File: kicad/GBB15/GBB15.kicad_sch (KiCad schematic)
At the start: 70 parts, among them J1 CAN_IN, J10 USB_C_Receptacle_USB2.0, J2 CAN_OUT, J3 M0_THERM, J4 M1_THERM, J5 Conn_01x04_Male, J6 Conn_01x04_Male, J7 ENDSTOP1, J8 ENDSTOP2, SW1 SW_Push, SW2 SW_Push, U1 TMC2209-LA-T, U2 STM32G0B1CEU6, U3 TMC2209-LA-T, U4 TCAN334, U5 NCP730BMT330TBG, Y1 Crystal_GND24

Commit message: PCB cleanup
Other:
- note added: "USB Type-C upright LCSC part#: C2763103 (1mm PCB) C3039300 C3039301 (1mm PCB) C3151747 C3151746"
- note removed: "Achtung mit UARTS im Bootloader Modus"
- note removed: "Motor A/B statt 0/1"
- note removed: "USB Type-C upright C2763103 (1mm PCB) C3039300 C3039301 (1mm PCB) C3151747 C3151746"
- note removed: "Umbennnen"
- note removed: "serial port"
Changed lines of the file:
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@@
-    (effects (font (size 1.27 1.27)) (justify left bottom))
-  )
-  (text "Motor A/B statt 0/1" (at 275.59 -13.97 0)
     (effects (font (size 1.27 1.27)) (justify left bottom))
   )
@@
   )
   (text "ADC" (at 246.38 146.05 0)
-    (effects (font (size 1.27 1.27)) (justify left bottom))
-  )
-  (text "serial port" (at 203.2 -26.67 0)
     (effects (font (size 1.27 1.27)) (justify left bottom))
   )
@@
   )
   (text "USART5_TX" (at 135.89 153.67 0)
-    (effects (font (size 1.27 1.27)) (justify left bottom))
-  )
-  (text "Umbennnen" (at 168.9067 -20.4934 0)
     (effects (font (size 1.27 1.27)) (justify left bottom))
   )
@@
     (effects (font (size 1.27 1.27)) (justify left bottom))
   )
-  (text "USB Type-C upright\nC2763103 (1mm PCB)\nC3039300\nC3039301 (1mm PCB)\nC3151747\nC3151746"
-    (at 214.63 -13.97 0)
+  (text "USB Type-C upright LCSC part#:\nC2763103 (1mm PCB)\nC3039300\nC3039301 (1mm PCB)\nC3151747\nC3151746"
+    (at 31.75 111.76 0)
     (effects (font (size 1.27 1.27)) (justify left bottom))
   )
@@
     (effects (font (size 1.27 1.27)) (justify left bottom))
   )
-  (text "Achtung mit UARTS im Bootloader Modus\n" (at 156.21 -2.54 0)
-    (effects (font (size 1.27 1.27)) (justify left bottom))
-  )

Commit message: Small changes in JST connector type
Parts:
- J5, J6: footprint Connector_JST:JST_XA_B04B-XASK-1_1x04_P2.50mm_Vertical -> Connector_JST:JST_XH_B4B-XH-A_1x04_P2.50mm_Vertical
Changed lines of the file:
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@@
       (effects (font (size 1.27 1.27)) (justify right))
     )
-    (property "Footprint" "Connector_JST:JST_XA_B04B-XASK-1_1x04_P2.50mm_Vertical" (id 2) (at 372.11 193.04 0)
+    (property "Footprint" "Connector_JST:JST_XH_B4B-XH-A_1x04_P2.50mm_Vertical" (id 2) (at 372.11 193.04 0)
       (effects (font (size 1.27 1.27)) hide)
     )
@@
       (effects (font (size 1.27 1.27)) (justify right))
     )
-    (property "Footprint" "Connector_JST:JST_XA_B04B-XASK-1_1x04_P2.50mm_Vertical" (id 2) (at 372.11 62.23 0)
+    (property "Footprint" "Connector_JST:JST_XH_B4B-XH-A_1x04_P2.50mm_Vertical" (id 2) (at 372.11 62.23 0)
       (effects (font (size 1.27 1.27)) hide)
     )
@@
     )
     (path "/9d8076e4-90bf-434d-b742-fd981c971465"
-      (reference "J5") (unit 1) (value "Conn_01x04_Male") (footprint "Connector_JST:JST_XA_B04B-XASK-1_1x04_P2.50mm_Vertical")
+      (reference "J5") (unit 1) (value "Conn_01x04_Male") (footprint "Connector_JST:JST_XH_B4B-XH-A_1x04_P2.50mm_Vertical")
     )
     (path "/3b24db73-62b8-474f-9981-d07b21e4d1b2"
-      (reference "J6") (unit 1) (value "Conn_01x04_Male") (footprint "Connector_JST:JST_XA_B04B-XASK-1_1x04_P2.50mm_Vertical")
+      (reference "J6") (unit 1) (value "Conn_01x04_Male") (footprint "Connector_JST:JST_XH_B4B-XH-A_1x04_P2.50mm_Vertical")
     )
     (path "/d1dfdd89-38c1-4297-bb44-8a8a1f194428"

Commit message: Added LCSC properties in schematic
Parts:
- C1, C17: LCSC (none) -> C3035369
- C10, C14, C22, C30: LCSC (none) -> C19666
- C11, C16, C18, C2, C21, C24, C26, C27, C28, C6, C7: LCSC (none) -> C57112
- C12, C15, C29, C8, C9: LCSC (none) -> C28323
- C13, C5: LCSC (none) -> C21122
- C3, C4: LCSC (none) -> C1653
- J1, J2: LCSC (none) -> C563821
- J10: LCSC (none) -> C3151747
- J3, J4, J7, J8: LCSC (none) -> C131337
- J5, J6: LCSC (none) -> C144395
- R1, R10, R2, R9: LCSC (none) -> C2934288
- R11, R12, R14, R20, R21, R22, R23, R5, R6: LCSC (none) -> C23162
- R13, R15: LCSC (none) -> C23186
- R16, R3, R4, R7, R8: LCSC (none) -> C25804
- R19: LCSC (none) -> C17909
- SW1, SW2: LCSC (none) -> C255802
- TH1: LCSC (none) -> C919169
- U1, U3: LCSC (none) -> C465949
- U2: LCSC (none) -> C2829190
- U4: LCSC (none) -> C165159
- U5: LCSC (none) -> C892821
- Y1: LCSC (none) -> C2682774

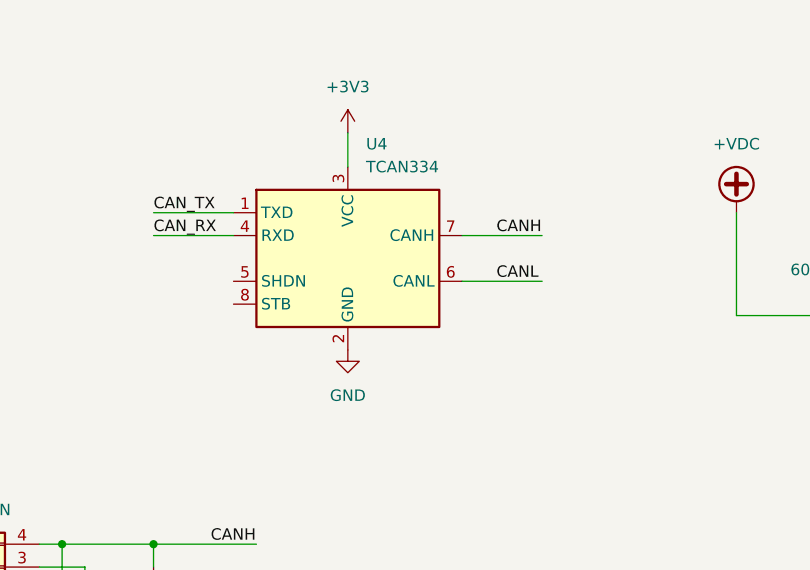
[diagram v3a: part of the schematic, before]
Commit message: Connected unconnected pads on TCAN334 to ground
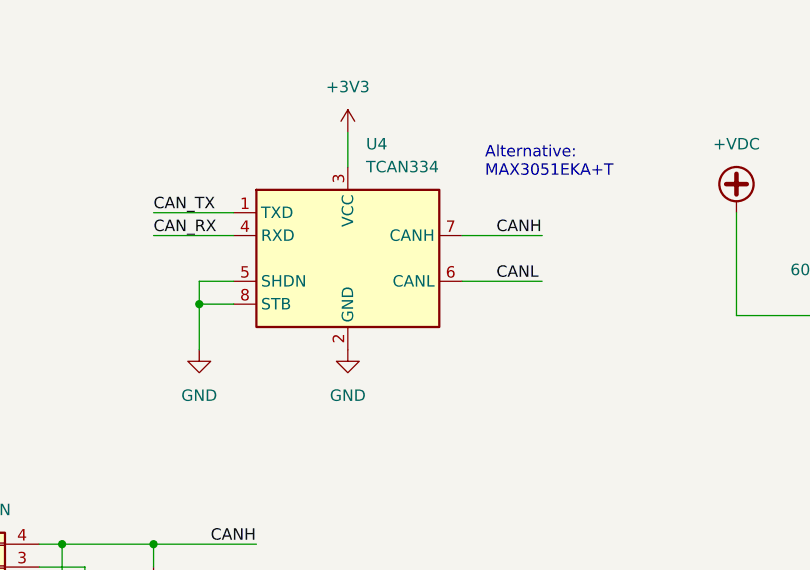
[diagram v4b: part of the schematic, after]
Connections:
- net GND: now also U4.5 (SHDN), U4.8 (STB)
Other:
- note added: "Alternative: MAX3051EKA+T"
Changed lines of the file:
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@@
   (junction (at 194.31 191.77) (diameter 0) (color 0 0 0 0)
   )
+  (junction (at 63.5 44.45) (diameter 0) (color 0 0 0 0)
+  )
   (junction (at 328.93 219.71) (diameter 0) (color 0 0 0 0)
   )
@@
     (stroke (width 0) (type default) (color 0 0 0 0))
   )
+  (wire (pts (xy 63.5 44.45) (xy 63.5 49.53))
+    (stroke (width 0) (type default) (color 0 0 0 0))
+  )
   (wire (pts (xy 48.26 71.12) (xy 58.42 71.12))
     (stroke (width 0) (type default) (color 0 0 0 0))
@@
     (stroke (width 0) (type default) (color 0 0 0 0))
   )
+  (wire (pts (xy 67.31 41.91) (xy 63.5 41.91))
+    (stroke (width 0) (type default) (color 0 0 0 0))
+  )
   (wire (pts (xy 344.17 154.94) (xy 344.17 156.21))
     (stroke (width 0) (type default) (color 0 0 0 0))
@@
     (stroke (width 0) (type default) (color 0 0 0 0))
   )
+  (wire (pts (xy 63.5 41.91) (xy 63.5 44.45))
+    (stroke (width 0) (type default) (color 0 0 0 0))
+  )
   (wire (pts (xy 292.1 72.39) (xy 295.91 72.39))
     (stroke (width 0) (type default) (color 0 0 0 0))
@@
     (stroke (width 0) (type default) (color 0 0 0 0))
   )
+  (wire (pts (xy 67.31 44.45) (xy 63.5 44.45))
+    (stroke (width 0) (type default) (color 0 0 0 0))
+  )
   (wire (pts (xy 303.53 64.77) (xy 311.15 64.77))
     (stroke (width 0) (type default) (color 0 0 0 0))
@@
     (effects (font (size 1.27 1.27)) (justify left bottom))
   )
+  (text "Alternative:\nMAX3051EKA+T" (at 95.25 30.48 0)
+    (effects (font (size 1.27 1.27)) (justify left bottom))
+  )
   (text "FDCAN2_RX" (at 152.4 146.05 0)
     (effects (font (size 1.27 1.27)) (justify left bottom))
@@
     (pin "1")
   )
+  (symbol (lib_id "power:GND") (at 63.5 49.53 0) (unit 1)
+    (in_bom yes) (on_board yes) (fields_autoplaced)
+    (property "Reference" "#PWR0164" (id 0) (at 63.5 55.88 0)
+      (effects (font (size 1.27 1.27)) hide)
+    )
+    (property "Value" "GND" (id 1) (at 63.5 54.61 0))
+    (property "Footprint" "" (id 2) (at 63.5 49.53 0)
+      (effects (font (size 1.27 1.27)) hide)
+    )
+    (property "Datasheet" "" (id 3) (at 63.5 49.53 0)
+      (effects (font (size 1.27 1.27)) hide)
+    )
+    (pin "1")
+  )
   (symbol (lib_id "Device:C") (at 354.33 160.02 180) (unit 1)
     (in_bom yes) (on_board yes)
@@
       (reference "#PWR0163") (unit 1) (value "+3V3") (footprint "")
     )
+    (path "/7c0fd88a-fa32-46d6-8af5-3806631ccf87"
+      (reference "#PWR0164") (unit 1) (value "GND") (footprint "")
+    )
     (path "/2357a709-2903-4077-9523-97359b4f842d"

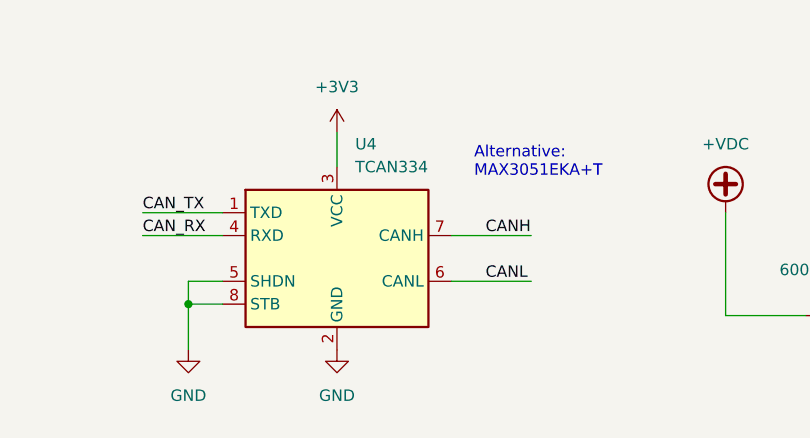
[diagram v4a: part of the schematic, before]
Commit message: Correct 100nF capacitor part number and changed to MAX3051 instead of TCAN334
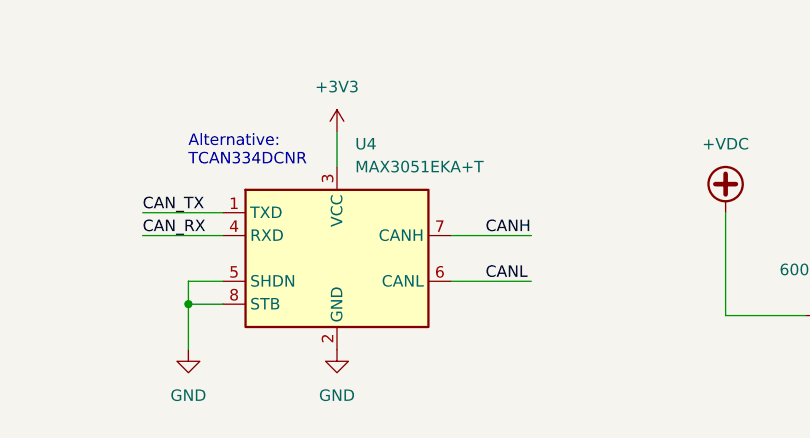
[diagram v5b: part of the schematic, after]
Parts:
- C11, C16, C18, C2, C21, C24, C26, C27, C28, C6, C7: LCSC C57112 -> C14663
- U4: value TCAN334 -> MAX3051EKA+T; LCSC C165159 -> C112005
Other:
- note added: "Alternative: TCAN334DCNR"
- note removed: "Alternative: MAX3051EKA+T"
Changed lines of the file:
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@@
     (effects (font (size 1.27 1.27)) (justify left bottom))
   )
-  (text "Alternative:\nMAX3051EKA+T" (at 95.25 30.48 0)
+  (text "Alternative:\nTCAN334DCNR\n" (at 63.5 29.21 0)
     (effects (font (size 1.27 1.27)) (justify left bottom))
   )
@@
       (effects (font (size 1.27 1.27)) hide)
     )
-    (property "LCSC" "C57112" (id 4) (at 118.11 123.19 0)
+    (property "LCSC" "C14663" (id 4) (at 118.11 123.19 0)
       (effects (font (size 1.27 1.27)) hide)
     )
@@
       (effects (font (size 1.27 1.27)) hide)
     )
-    (property "LCSC" "C57112" (id 4) (at 307.34 35.56 0)
+    (property "LCSC" "C14663" (id 4) (at 307.34 35.56 0)
       (effects (font (size 1.27 1.27)) hide)
     )
@@
       (effects (font (size 1.27 1.27)) (justify left))
     )
-    (property "Value" "TCAN334" (id 1) (at 82.0294 29.21 0)
+    (property "Value" "MAX3051EKA+T" (id 1) (at 82.0294 29.21 0)
       (effects (font (size 1.27 1.27)) (justify left))
     )
@@
       (effects (font (size 1.27 1.27)) hide)
     )
-    (property "LCSC" "C165159" (id 4) (at 82.0294 26.67 0)
+    (property "LCSC" "C112005" (id 4) (at 82.0294 26.67 0)
       (effects (font (size 1.27 1.27)) hide)
     )
@@
       (effects (font (size 1.27 1.27)) hide)
     )
-    (property "LCSC" "C57112" (id 4) (at 347.98 132.08 0)
+    (property "LCSC" "C14663" (id 4) (at 347.98 132.08 0)
       (effects (font (size 1.27 1.27)) hide)
     )
@@
       (effects (font (size 1.27 1.27)) hide)
     )
-    (property "LCSC" "C57112" (id 4) (at 128.27 123.19 0)
+    (property "LCSC" "C14663" (id 4) (at 128.27 123.19 0)
       (effects (font (size 1.27 1.27)) hide)
     )
@@
       (effects (font (size 1.27 1.27)) hide)
     )
-    (property "LCSC" "C57112" (id 4) (at 293.37 132.08 0)
+    (property "LCSC" "C14663" (id 4) (at 293.37 132.08 0)
       (effects (font (size 1.27 1.27)) hide)
     )
@@
       (effects (font (size 1.27 1.27)) hide)
     )
-    (property "LCSC" "C57112" (id 4) (at 72.39 242.57 0)
+    (property "LCSC" "C14663" (id 4) (at 72.39 242.57 0)
       (effects (font (size 1.27 1.27)) hide)
     )
@@
       (effects (font (size 1.27 1.27)) hide)
     )
-    (property "LCSC" "C57112" (id 4) (at 365.76 45.72 0)
+    (property "LCSC" "C14663" (id 4) (at 365.76 45.72 0)
       (effects (font (size 1.27 1.27)) hide)
     )
@@
       (effects (font (size 1.27 1.27)) hide)
     )
-    (property "LCSC" "C57112" (id 4) (at 72.39 201.93 0)
+    (property "LCSC" "C14663" (id 4) (at 72.39 201.93 0)
       (effects (font (size 1.27 1.27)) hide)
     )
@@
       (effects (font (size 1.27 1.27)) hide)
     )
-    (property "LCSC" "C57112" (id 4) (at 365.76 176.53 0)
+    (property "LCSC" "C14663" (id 4) (at 365.76 176.53 0)
       (effects (font (size 1.27 1.27)) hide)
     )
@@
       (effects (font (size 1.27 1.27)) hide)
     )
-    (property "LCSC" "C57112" (id 4) (at 307.34 166.37 0)
+    (property "LCSC" "C14663" (id 4) (at 307.34 166.37 0)
       (effects (font (size 1.27 1.27)) hide)
     )
@@
       (effects (font (size 1.27 1.27)) hide)
     )
-    (property "LCSC" "C57112" (id 4) (at 125.73 158.75 0)
+    (property "LCSC" "C14663" (id 4) (at 125.73 158.75 0)
       (effects (font (size 1.27 1.27)) hide)
     )
@@
     )
     (path "/1bcdfb0e-7d1c-413c-9751-c956c1d9a4e0"
-      (reference "U4") (unit 1) (value "TCAN334") (footprint "Package_TO_SOT_SMD:SOT-23-8")
+      (reference "U4") (unit 1) (value "MAX3051EKA+T") (footprint "Package_TO_SOT_SMD:SOT-23-8")
     )
     (path "/bab8dc9b-0be7-4bfb-810b-951e3d411197"

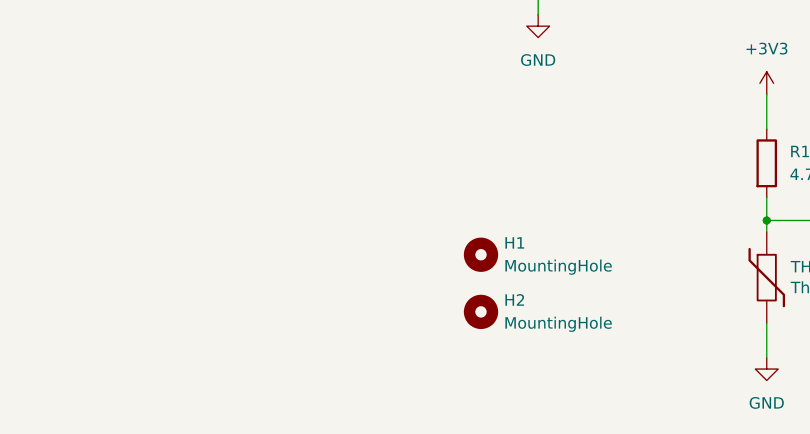
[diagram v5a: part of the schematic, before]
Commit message: Added tooling holes
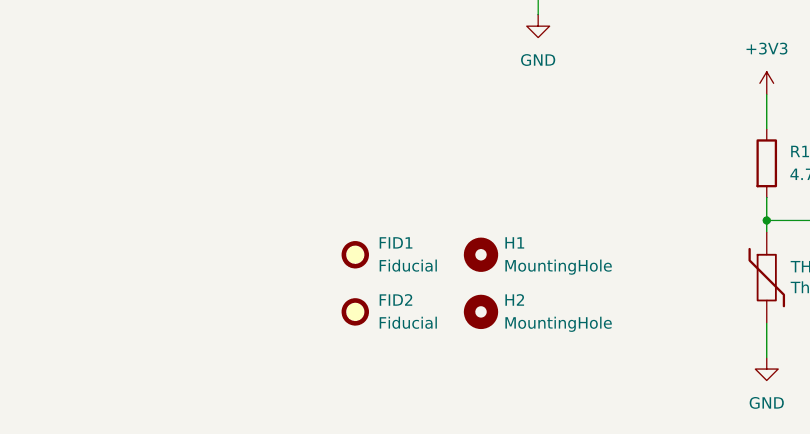
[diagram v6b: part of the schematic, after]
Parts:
- added FID1, FID2: Fiducial, Project:TOOLING-HOLE, symbol Mechanical:Fiducial
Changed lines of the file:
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@@
     (pin "2")
+  )
+  (symbol (lib_id "Mechanical:Fiducial") (at 157.48 256.54 0) (unit 1)
+    (in_bom yes) (on_board yes) (fields_autoplaced)
+    (property "Reference" "FID2" (id 0) (at 160.02 255.2699 0)
+      (effects (font (size 1.27 1.27)) (justify left))
+    )
+    (property "Value" "Fiducial" (id 1) (at 160.02 257.8099 0)
+      (effects (font (size 1.27 1.27)) (justify left))
+    )
+    (property "Footprint" "Project:TOOLING-HOLE" (id 2) (at 157.48 256.54 0)
+      (effects (font (size 1.27 1.27)) hide)
+    )
+    (property "Datasheet" "~" (id 3) (at 157.48 256.54 0)
+      (effects (font (size 1.27 1.27)) hide)
+    )
   )
   (symbol (lib_id "Device:C") (at 124.46 116.84 180) (unit 1)
@@
     (pin "2")
   )
+  (symbol (lib_id "Mechanical:Fiducial") (at 157.48 250.19 0) (unit 1)
+    (in_bom yes) (on_board yes) (fields_autoplaced)
+    (property "Reference" "FID1" (id 0) (at 160.02 248.9199 0)
+      (effects (font (size 1.27 1.27)) (justify left))
+    )
+    (property "Value" "Fiducial" (id 1) (at 160.02 251.4599 0)
+      (effects (font (size 1.27 1.27)) (justify left))
+    )
+    (property "Footprint" "Project:TOOLING-HOLE" (id 2) (at 157.48 250.19 0)
+      (effects (font (size 1.27 1.27)) hide)
+    )
+    (property "Datasheet" "~" (id 3) (at 157.48 250.19 0)
+      (effects (font (size 1.27 1.27)) hide)
+    )
+  )
   (symbol (lib_id "power:GND") (at 360.68 90.17 0) (unit 1)
     (in_bom yes) (on_board yes) (fields_autoplaced)
@@
       (reference "FB1") (unit 1) (value "600R@100MHz") (footprint "Inductor_SMD:L_0603_1608Metric")
     )
+    (path "/c7406de1-a71d-4f7a-80e6-d8c8875ed536"
+      (reference "FID1") (unit 1) (value "Fiducial") (footprint "Project:TOOLING-HOLE")
+    )
+    (path "/0662f878-ff9c-493f-9caa-fd70364c8986"
+      (reference "FID2") (unit 1) (value "Fiducial") (footprint "Project:TOOLING-HOLE")
+    )
     (path "/77342960-d5c8-47dc-8112-7bc87dec7f3d"
